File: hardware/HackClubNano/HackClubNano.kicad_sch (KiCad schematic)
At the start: 0 parts

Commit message: Continued the tutorial with the schematics info.
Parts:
- added R1, R2: 27.4, symbol Device:R
- added U1: RP2040, Package_DFN_QFN:QFN-56-1EP_7x7mm_P0.4mm_EP3.2x3.2mm, symbol MCU_RaspberryPi:RP2040
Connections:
- new net: U1.1 (IOVDD), U1.10 (IOVDD), U1.22 (IOVDD), U1.33 (IOVDD), U1.42 (IOVDD), U1.49 (IOVDD)
- new net: U1.23 (DVDD), U1.50 (DVDD)
- new net: R2.2, U1.46 (USB_DM)
- new net: R1.2, U1.47 (USB_DP)
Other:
- title: (none) -> Hack Club Nano

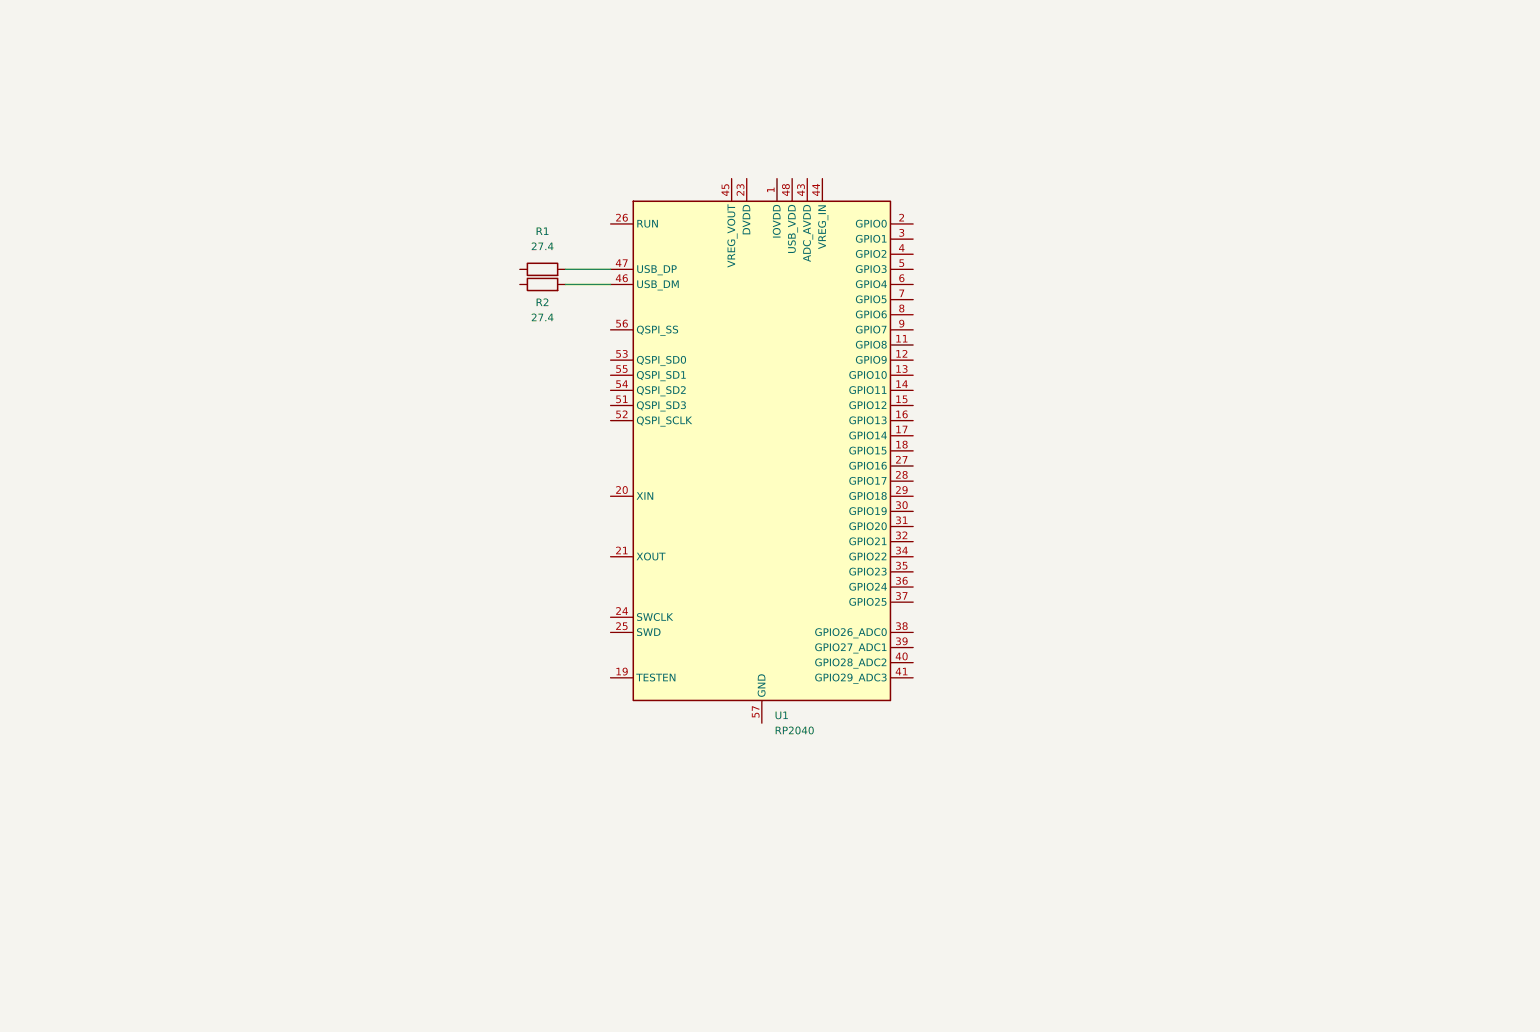
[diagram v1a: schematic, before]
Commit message: Added the usb and the power guides.
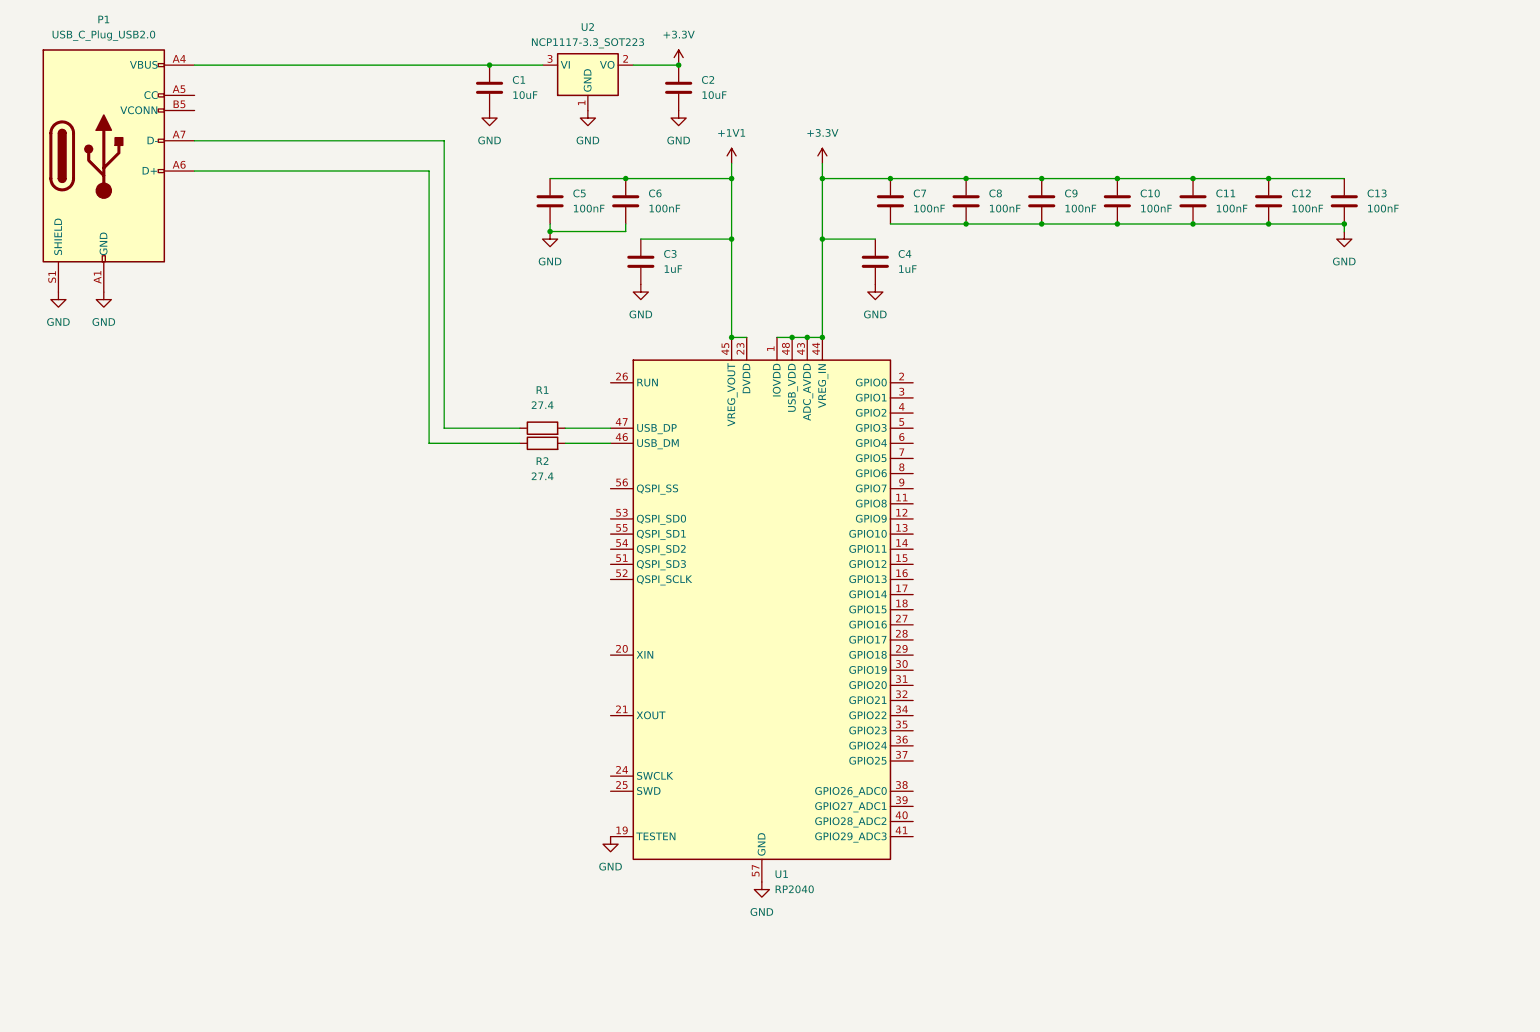
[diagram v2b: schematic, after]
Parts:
- added C1, C2: 10uF, symbol Device:C
- added C10, C11, C12, C13, C5, C6, C7, C8, C9: 100nF, symbol Device:C
- added C3, C4: 1uF, symbol Device:C
- added P1: USB_C_Plug_USB2.0, symbol Connector:USB_C_Plug_USB2.0
- added U2: NCP1117-3.3_SOT223, Package_TO_SOT_SMD:SOT-223-3_TabPin2, symbol Regulator_Linear:NCP1117-3.3_SOT223
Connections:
- net +3.3V: now reaches U1.1 (IOVDD), U1.10 (IOVDD), U1.22 (IOVDD), U1.33 (IOVDD), U1.42 (IOVDD), U1.49 (IOVDD)
- net +3.3V: now also U1.43 (ADC_AVDD), U1.44 (VREG_IN), U1.48 (USB_VDD), C10.1, C11.1, C12.1, C13.1, C2.1, C4.1, C7.1, C8.1, C9.1, U2.2 (VO)
- net GND: now reaches U1.19 (TESTEN)
- net GND: now also U1.57 (GND), C1.2, C10.2, C11.2, C12.2, C13.2, C2.2, C3.2, C4.2, C5.2, C6.2, C7.2, C8.2, C9.2, P1.A1 (GND), P1.A12 (GND), P1.B1 (GND), P1.B12 (GND), P1.S1 (SHIELD), U2.1 (GND)
- net +1V1: now reaches U1.23 (DVDD), U1.50 (DVDD)
- net +1V1: now also U1.45 (VREG_VOUT), C3.1, C5.1, C6.1
- net at R2.1: now also P1.A6 (D+)
- net at R1.1: now also P1.A7 (D-)
- new net: C1.1, P1.A4 (VBUS), P1.A9 (VBUS), P1.B4 (VBUS), P1.B9 (VBUS), U2.3 (VI)
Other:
- moved on the sheet: R1, R2, U1

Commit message: Made the flash, the crystal and the io pins guides.
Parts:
- added C14: 100nF, symbol Device:C
- added C15, C16: 15pF, symbol Device:C
- added J1, J3: Conn_01x18, symbol Connector_Generic:Conn_01x18
- added J2: Conn_01x02, symbol Connector_Generic:Conn_01x02
- added R3, R5: 1k, symbol Device:R
- added R4: 0 | 10k, symbol Device:R
- added U3: W25Q128JVS, Package_SO:SOIC-8_5.3x5.3mm_P1.27mm, symbol Memory_Flash:W25Q128JVS
- added Y1: Crystal_GND24, symbol Device:Crystal_GND24
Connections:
- net +3.3V: now also C14.1, J1.1 (Pin_1), R4.1, U3.8 (VCC)
- net GND: now also C14.2, C15.2, C16.1, J1.18 (Pin_18), J2.1 (Pin_1), J3.18 (Pin_18), U3.4 (GND), Y1.2, Y1.4
- net GPIO8: now reaches U1.11 (GPIO8)
- net GPIO8: now also J1.10 (Pin_10)
- net GPIO9: now reaches U1.12 (GPIO9)
- net GPIO9: now also J1.11 (Pin_11)
- net GPIO10: now reaches U1.13 (GPIO10)
- net GPIO10: now also J1.12 (Pin_12)
- net GPIO11: now reaches U1.14 (GPIO11)
- net GPIO11: now also J1.13 (Pin_13)
- net GPIO12: now reaches U1.15 (GPIO12)
- net GPIO12: now also J1.14 (Pin_14)
- net GPIO13: now reaches U1.16 (GPIO13)
- net GPIO13: now also J1.15 (Pin_15)
- net GPIO14: now reaches U1.17 (GPIO14)
- net GPIO14: now also J1.16 (Pin_16)
- net GPIO15: now reaches U1.18 (GPIO15)
- net GPIO15: now also J1.17 (Pin_17)
- net GPIO0: now reaches U1.2 (GPIO0)
- net GPIO0: now also J1.2 (Pin_2)
- net at U1.20 (XIN): now also C16.2, Y1.1
- net at U1.21 (XOUT): now also R5.2
- net SWCLK: now reaches U1.24 (SWCLK)
- net SWCLK: now also J3.16 (Pin_16)
- net SWD: now reaches U1.25 (SWD)
- net SWD: now also J3.17 (Pin_17)
- net RUN: now reaches U1.26 (RUN)
- net RUN: now also J3.15 (Pin_15)
- net GPIO16: now reaches U1.27 (GPIO16)
- net GPIO16: now also J3.14 (Pin_14)
- net GPIO17: now reaches U1.28 (GPIO17)
- net GPIO17: now also J3.13 (Pin_13)
- net GPIO18: now reaches U1.29 (GPIO18)
- net GPIO18: now also J3.12 (Pin_12)
- net GPIO1: now reaches U1.3 (GPIO1)
- net GPIO1: now also J1.3 (Pin_3)
- net GPIO19: now reaches U1.30 (GPIO19)
- net GPIO19: now also J3.11 (Pin_11)
- net GPIO20: now reaches U1.31 (GPIO20)
- net GPIO20: now also J3.10 (Pin_10)
- net GPIO21: now reaches U1.32 (GPIO21)
- net GPIO21: now also J3.9 (Pin_9)
- net GPIO22: now reaches U1.34 (GPIO22)
- net GPIO22: now also J3.8 (Pin_8)
- net GPIO23: now reaches U1.35 (GPIO23)
- net GPIO23: now also J3.7 (Pin_7)
- net GPIO24: now reaches U1.36 (GPIO24)
- net GPIO24: now also J3.6 (Pin_6)
- net GPIO25: now reaches U1.37 (GPIO25)
- net GPIO25: now also J3.5 (Pin_5)
- net GPIO26_ADC0: now reaches U1.38 (GPIO26_ADC0)
- net GPIO26_ADC0: now also J3.4 (Pin_4)
- net GPIO27_ADC1: now reaches U1.39 (GPIO27_ADC1)
- net GPIO27_ADC1: now also J3.3 (Pin_3)
- net GPIO2: now reaches U1.4 (GPIO2)
- net GPIO2: now also J1.4 (Pin_4)
- net GPIO28_ADC2: now reaches U1.40 (GPIO28_ADC2)
- net GPIO28_ADC2: now also J3.2 (Pin_2)
- net GPIO28_ADC3: now reaches U1.41 (GPIO29_ADC3)
- net GPIO28_ADC3: now also J3.1 (Pin_1)
- net GPIO3: now reaches U1.5 (GPIO3)
- net GPIO3: now also J1.5 (Pin_5)
- net at U1.51 (QSPI_SD3): now also U3.7 (~{HOLD}/~{RESET}/IO_{3})
- net at U1.52 (QSPI_SCLK): now also U3.6 (CLK)
- net at U1.53 (QSPI_SD0): now also U3.5 (DI/IO_{0})
- net at U1.54 (QSPI_SD2): now also U3.3 (~{WP}/IO_{2})
- net at U1.55 (QSPI_SD1): now also U3.2 (DO/IO_{1})
- net at U1.56 (QSPI_SS): now also R3.2, R4.2, U3.1 (~{CS})
- net GPIO4: now reaches U1.6 (GPIO4)
- net GPIO4: now also J1.6 (Pin_6)
- net GPIO5: now reaches U1.7 (GPIO5)
- net GPIO5: now also J1.7 (Pin_7)
- net GPIO6: now reaches U1.8 (GPIO6)
- net GPIO6: now also J1.8 (Pin_8)
- net GPIO7: now reaches U1.9 (GPIO7)
- net GPIO7: now also J1.9 (Pin_9)
- new net: C15.1, R5.1, Y1.3
- new net: J2.2 (Pin_2), R3.1

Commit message: Started the PCB tutorial.
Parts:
- C1, C10, C11, C12, C13, C14, C15, C16, C2, C3, C4, C5, C6, C7, C8, C9: footprint (none) -> Capacitor_SMD:C_0603_1608Metric
- J1, J3: footprint (none) -> Connector_PinHeader_2.00mm:PinHeader_1x18_P2.00mm_Vertical
- J2: footprint (none) -> Connector_PinHeader_2.00mm:PinHeader_1x02_P2.00mm_Vertical
- P1: footprint (none) -> Connector_USB:USB_C_Receptacle_HRO_TYPE-C-31-M-12
- R1, R2, R3, R4, R5: footprint (none) -> Resistor_THT:R_Axial_DIN0207_L6.3mm_D2.5mm_P7.62mm_Horizontal
- Y1: footprint (none) -> Crystal:Crystal_HC49-4H_Vertical
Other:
- company: (none) -> Hack Club RedBoard
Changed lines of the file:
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@@
 	(title_block
 		(title "Hack Club Nano")
-		(date "2026-04-08")
+		(date "2026-04-09")
+		(company "Hack Club RedBoard")
 	)
 	(junction
@@
 			)
 		)
-		(property "Footprint" ""
+		(property "Footprint" "Capacitor_SMD:C_0603_1608Metric"
 			(at 227.0252 50.8 0)
 			(effects
@@
 			)
 		)
-		(property "Footprint" ""
+		(property "Footprint" "Capacitor_SMD:C_0603_1608Metric"
 			(at 83.5152 113.03 0)
 			(effects
@@
 			)
 		)
-		(property "Footprint" ""
+		(property "Footprint" "Crystal:Crystal_HC49-4H_Vertical"
 			(at 87.63 171.45 0)
 			(effects
@@
 			)
 		)
-		(property "Footprint" ""
+		(property "Footprint" "Capacitor_SMD:C_0603_1608Metric"
 			(at 188.9252 50.8 0)
 			(effects
@@
 			)
 		)
-		(property "Footprint" ""
+		(property "Footprint" "Connector_PinHeader_2.00mm:PinHeader_1x02_P2.00mm_Vertical"
 			(at 21.59 124.46 0)
 			(effects
@@
 			)
 		)
-		(property "Footprint" ""
+		(property "Footprint" "Connector_USB:USB_C_Receptacle_HRO_TYPE-C-31-M-12"
 			(at 34.29 39.37 0)
 			(effects
@@
 			)
 		)
-		(property "Footprint" ""
+		(property "Footprint" "Capacitor_SMD:C_0603_1608Metric"
 			(at 96.2152 31.75 0)
 			(effects
@@
 			)
 		)
-		(property "Footprint" ""
+		(property "Footprint" "Resistor_THT:R_Axial_DIN0207_L6.3mm_D2.5mm_P7.62mm_Horizontal"
 			(at 104.14 89.408 90)
 			(effects
@@
 			)
 		)
-		(property "Footprint" ""
+		(property "Footprint" "Connector_PinHeader_2.00mm:PinHeader_1x18_P2.00mm_Vertical"
 			(at 254 105.41 0)
 			(effects
@@
 			)
 		)
-		(property "Footprint" ""
+		(property "Footprint" "Resistor_THT:R_Axial_DIN0207_L6.3mm_D2.5mm_P7.62mm_Horizontal"
 			(at 36.83 123.698 90)
 			(effects
@@
 			)
 		)
-		(property "Footprint" ""
+		(property "Footprint" "Capacitor_SMD:C_0603_1608Metric"
 			(at 201.6252 50.8 0)
 			(effects
@@
 			)
 		)
-		(property "Footprint" ""
+		(property "Footprint" "Capacitor_SMD:C_0603_1608Metric"
 			(at 106.3752 50.8 0)
 			(effects
@@
 			)
 		)
-		(property "Footprint" ""
+		(property "Footprint" "Capacitor_SMD:C_0603_1608Metric"
 			(at 163.5252 50.8 0)
 			(effects
@@
 			)
 		)
-		(property "Footprint" ""
+		(property "Footprint" "Connector_PinHeader_2.00mm:PinHeader_1x18_P2.00mm_Vertical"
 			(at 217.17 105.41 0)
 			(effects
@@
 			)
 		)
-		(property "Footprint" ""
+		(property "Footprint" "Capacitor_SMD:C_0603_1608Metric"
 			(at 214.3252 50.8 0)
 			(effects
@@
 			)
 		)
-		(property "Footprint" ""
+		(property "Footprint" "Capacitor_SMD:C_0603_1608Metric"
 			(at 239.7252 50.8 0)
 			(effects
@@
 			)
 		)
-		(property "Footprint" ""
+		(property "Footprint" "Capacitor_SMD:C_0603_1608Metric"
 			(at 127.9652 31.75 0)
 			(effects
@@
 			)
 		)
-		(property "Footprint" ""
+		(property "Footprint" "Capacitor_SMD:C_0603_1608Metric"
 			(at 176.2252 50.8 0)
 			(effects
@@
 			)
 		)
-		(property "Footprint" ""
+		(property "Footprint" "Capacitor_SMD:C_0603_1608Metric"
 			(at 71.12 176.2252 0)
 			(effects
@@
 			)
 		)
-		(property "Footprint" ""
+		(property "Footprint" "Resistor_THT:R_Axial_DIN0207_L6.3mm_D2.5mm_P7.62mm_Horizontal"
 			(at 104.14 86.868 90)
 			(effects
@@
 			)
 		)
-		(property "Footprint" ""
+		(property "Footprint" "Capacitor_SMD:C_0603_1608Metric"
 			(at 160.9852 60.96 0)
 			(effects
@@
 			)
 		)
-		(property "Footprint" ""
+		(property "Footprint" "Capacitor_SMD:C_0603_1608Metric"
 			(at 121.6152 60.96 0)
 			(effects
@@
 			)
 		)
-		(property "Footprint" ""
+		(property "Footprint" "Capacitor_SMD:C_0603_1608Metric"
 			(at 78.74 166.6748 0)
 			(effects
@@
 			)
 		)
-		(property "Footprint" ""
+		(property "Footprint" "Resistor_THT:R_Axial_DIN0207_L6.3mm_D2.5mm_P7.62mm_Horizontal"
 			(at 100.33 177.038 90)
 			(effects
@@
 			)
 		)
-		(property "Footprint" ""
+		(property "Footprint" "Resistor_THT:R_Axial_DIN0207_L6.3mm_D2.5mm_P7.62mm_Horizontal"
 			(at 46.482 118.11 90)
 			(effects
@@
 			)
 		)
-		(property "Footprint" ""
+		(property "Footprint" "Capacitor_SMD:C_0603_1608Metric"
 			(at 119.0752 50.8 0)
 			(effects

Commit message: Finished the pcb guide. Finished the Hack Club Nano board.
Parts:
- Y1: footprint Crystal:Crystal_HC49-4H_Vertical -> Crystal:Crystal_SMD_5032-4Pin_5.0x3.2mm
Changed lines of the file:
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@@
 			)
 		)
-		(property "Footprint" "Crystal:Crystal_HC49-4H_Vertical"
+		(property "Footprint" "Crystal:Crystal_SMD_5032-4Pin_5.0x3.2mm"
 			(at 87.63 171.45 0)
 			(effects
